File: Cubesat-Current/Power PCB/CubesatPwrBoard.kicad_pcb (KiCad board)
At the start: 2 copper layers, 90 x 96 mm, 92 parts, among them J1 Conn_01x04_Female, J10 S1, J11 S2, J12 S3, J13 S4, J14 S5, J15 S6, J2 Conn_01x04_Female, J3 Conn_01x04_Female, J5 Conn_01x04_Female, J6 Conn_01x03_Female, J7 Conn_01x03_Female, J8 Conn_01x03_Female, Q1 TQM110NB04CR_RLG, Q2 2N7002*, Q3 TQM110NB04CR_RLG, Q4 2N7002*, Q5 TQM110NB04CR_RLG, Q6 2N7002*, U1 LTC4162, U2 LTC4162, U3 LTC4162, U5 MAX710ESE+T, U6 MAX710ESE+T, U7 MAX710ESE+T

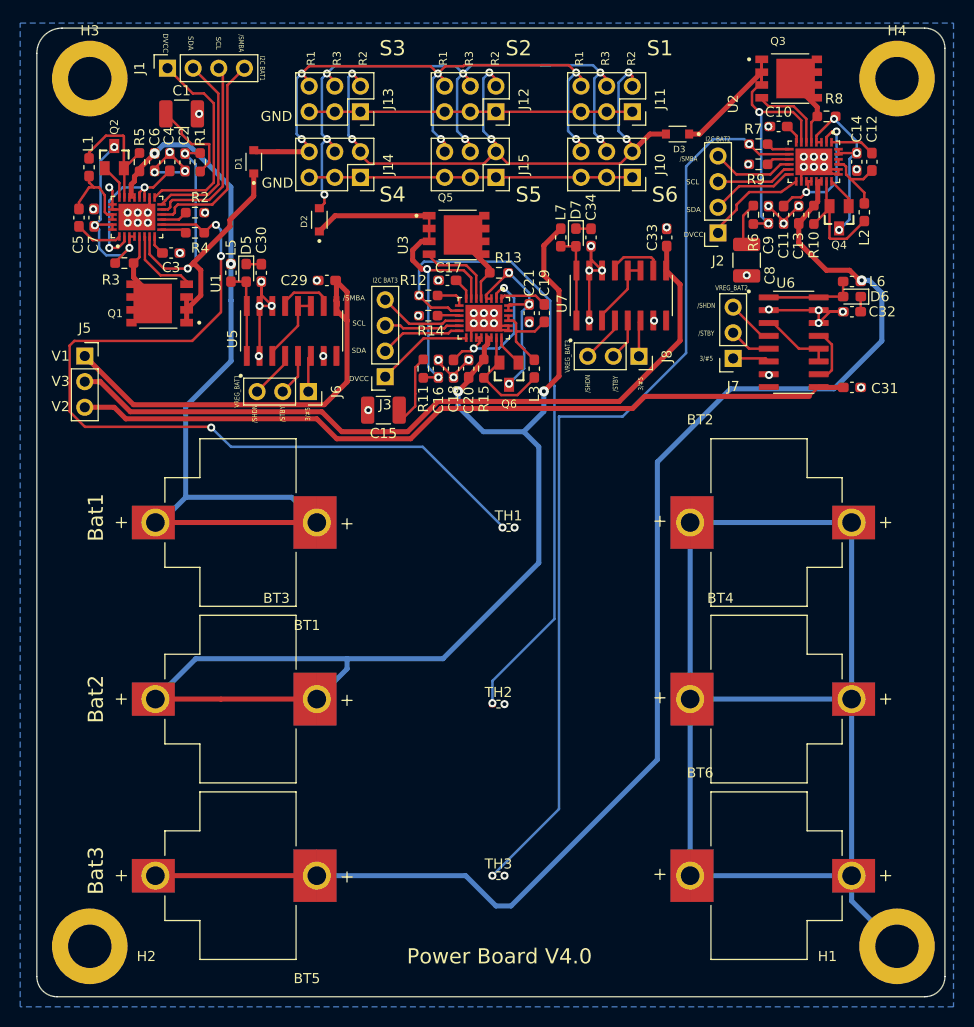
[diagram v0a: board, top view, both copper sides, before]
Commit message: Changed mounting holes to 4.2mm diameter and added silkscreen text
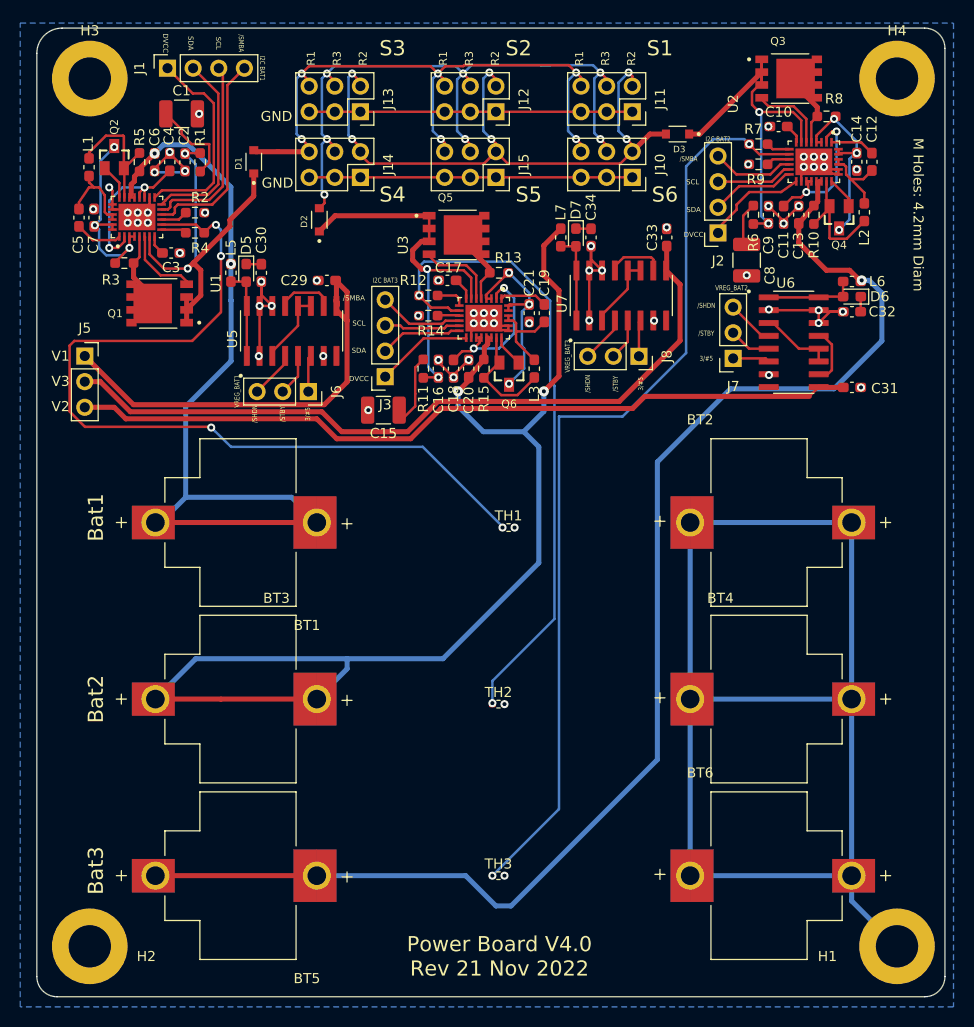
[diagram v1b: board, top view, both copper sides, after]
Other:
- board text added: "M Holes: 4.2mm Diam"
- board text added: "Power Board V4.0 Rev 21 Nov 2022"
- board text removed: "Power Board V4.0"
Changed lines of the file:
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@@
     (fp_circle (center 0 0) (end 3.75 0) (layer "Cmts.User") (width 0.15) (fill none))
     (fp_circle (center 0 0) (end 4 0) (layer "F.CrtYd") (width 0.05) (fill none))
-    (pad "1" thru_hole circle (at 0 0) (size 7.5 7.5) (drill 4.3) (layers *.Cu *.Paste *.Mask)
+    (pad "1" thru_hole circle (at 0 0) (size 7.5 7.5) (drill 4.2) (layers *.Cu *.Paste *.Mask)
       (net 2 "GND") (pinfunction "1") (pintype "input"))
   )
@@
     (fp_circle (center 0 0) (end 3.75 0) (layer "Cmts.User") (width 0.15) (fill none))
     (fp_circle (center 0 0) (end 4 0) (layer "F.CrtYd") (width 0.05) (fill none))
-    (pad "1" thru_hole circle (at 0 0) (size 7.5 7.5) (drill 4.3) (layers *.Cu *.Paste *.Mask)
+    (pad "1" thru_hole circle (at 0 0) (size 7.5 7.5) (drill 4.2) (layers *.Cu *.Paste *.Mask)
       (net 2 "GND") (pinfunction "1") (pintype "input"))
   )
@@
     (fp_circle (center 0 0) (end 3.75 0) (layer "Cmts.User") (width 0.15) (fill none))
     (fp_circle (center 0 0) (end 4 0) (layer "F.CrtYd") (width 0.05) (fill none))
-    (pad "1" thru_hole circle (at 0 0) (size 7.5 7.5) (drill 4.3) (layers *.Cu *.Paste *.Mask)
+    (pad "1" thru_hole circle (at 0 0) (size 7.5 7.5) (drill 4.2) (layers *.Cu *.Paste *.Mask)
       (net 2 "GND") (pinfunction "1") (pintype "input"))
   )
@@
     (fp_circle (center 0 0) (end 3.75 0) (layer "Cmts.User") (width 0.15) (fill none))
     (fp_circle (center 0 0) (end 4 0) (layer "F.CrtYd") (width 0.05) (fill none))
-    (pad "1" thru_hole circle (at 0 0) (size 7.5 7.5) (drill 4.3) (layers *.Cu *.Paste *.Mask)
+    (pad "1" thru_hole circle (at 0 0) (size 7.5 7.5) (drill 4.2) (layers *.Cu *.Paste *.Mask)
       (net 2 "GND") (pinfunction "1") (pintype "input"))
   )
@@
     (effects (font (size 0.5 0.5) (thickness 0.125)))
   )
-  (gr_text "Power Board V4.0" (at 152.5 137.5) (layer "F.SilkS")
+  (gr_text "Power Board V4.0\nRev 21 Nov 2022" (at 152.5 137.5) (layer "F.SilkS")
     (effects (font (size 1.5 1.5) (thickness 0.3)))
   )
@@
     (effects (font (size 0.5 0.4) (thickness 0.1)))
   )
+  (gr_text "M Holes: 4.2mm Diam" (at 194 64 270) (layer "F.SilkS")
+    (effects (font (size 1 1) (thickness 0.15)))
+  )
   (gr_text "3/#5" (at 166.5 80.75 90) (layer "F.SilkS")

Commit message: Updating to revision 5.0
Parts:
- removed BT1, BT2, BT3, BT4: 254TR, 254TR:BAT_254TR
- removed C19: C, Capacitor_SMD:C_0603_1608Metric_Pad1.08x0.95mm_HandSolder
- removed C20, C21: 10u, Capacitor_SMD:C_0603_1608Metric_Pad1.08x0.95mm_HandSolder
- removed C29, C30: C_Polarized_US, Capacitor_SMD:C_0603_1608Metric_Pad1.08x0.95mm_HandSolder
- removed C31, C33: 4.7u, Capacitor_SMD:C_0603_1608Metric_Pad1.08x0.95mm_HandSolder
- removed C32, C34: 100u, Capacitor_SMD:C_0603_1608Metric_Pad1.08x0.95mm_HandSolder
- removed the D2 at (134.7, 64.5)
- removed D5, D6, D7: D_Schottky, Diode_SMD:D_0603_1608Metric_Pad1.05x0.95mm_HandSolder
- removed the J5 at (111.4, 78.0)
- removed the J6 at (133.6, 81.5)
- removed L5: L, Inductor_SMD:L_0603_1608Metric_Pad1.05x0.95mm_HandSolder
- removed L6, L7: 22u, Inductor_SMD:L_0603_1608Metric_Pad1.05x0.95mm_HandSolder
- removed Q5: TQM110NB04CR_RLG, TQM110N:TRANS_TQM110NB04CR_RLG
- removed Q6: 2N7002*, 2N7002:SOT23
- removed R11: 2.5, Resistor_SMD:R_0603_1608Metric_Pad0.98x0.95mm_HandSolder
- removed R12, R13: 16m, Resistor_SMD:R_0603_1608Metric_Pad0.98x0.95mm_HandSolder
- removed R14: 63.4k, Resistor_SMD:R_0603_1608Metric_Pad0.98x0.95mm_HandSolder
- removed R15: 10m, Resistor_SMD:R_0603_1608Metric_Pad0.98x0.95mm_HandSolder
- removed the TH2 at (152.4, 112.5)
- removed U5, U6, U7: MAX710ESE+T, MAX710ESE:SOIC127P600X175-16N
- added D3: D_Schottky, Connectors_Cubesat_Custom:CubeSat_Diode_SOT_882, F.Cu at (139.4, 71.2)
- added D4: D_Schottky, Connectors_Cubesat_Custom:CubeSat_Diode_SOT_882, F.Cu at (183.1, 69.8)
- added J4: 254TR, 254TR:BAT_254TR, F.Cu at (178.5, 105.0)
- added J9: Conn_01x02_Female, Connectors_Cubesat_Custom:CubeSat_Conn_2x01_P2.54mm, F.Cu at (180.0, 53.0)
- added L4: 22u, Inductor_SMD:L_0603_1608Metric_Pad1.05x0.95mm_HandSolder, F.Cu at (180.6, 69.8)
- added U4: MAX710ESE+T, MAX710ESE:SOIC127P600X175-16N, F.Cu at (187.3, 79.6)
- C1: value C_Polarized_US -> 150u
- C12, C5: value C -> 22n
- C15: value 150u -> 4.7u; footprint Capacitor_SMD:C_1210_3225Metric_Pad1.33x2.70mm_HandSolder -> Capacitor_SMD:C_0603_1608Metric_Pad1.08x0.95mm_HandSolder
- C16: value C_Polarized_US -> 100u; footprint Capacitor_SMD:C_0603_1608Metric_Pad1.08x0.95mm_HandSolder -> Capacitor_SMD:C_0805_2012Metric_Pad1.18x1.45mm_HandSolder
- C17: value 1u -> 4.7u
- C18: value 4.7u -> 100u; footprint Capacitor_SMD:C_0603_1608Metric_Pad1.08x0.95mm_HandSolder -> Capacitor_SMD:C_0805_2012Metric_Pad1.18x1.45mm_HandSolder
- C2, C9: value C_Polarized_US -> 0.1u
- C3: value C -> 1u
- C4: value C -> 4.7u
- C6, C7: value C -> 10u
- D1: footprint CUS520,H3F:DIO_CUS520,H3F -> Connectors_Cubesat_Custom:CubeSat_DIO_CUS520,H3f
- D2: renamed from D3; footprint CUS520,H3F:DIO_CUS520,H3F -> Connectors_Cubesat_Custom:CubeSat_DIO_CUS520,H3f
- H1: renamed from H2; footprint MountingHole:MountingHole_4.3mm_M4_DIN965_Pad -> Connectors_Cubesat_Custom:CubeSat_MountingHole_M4
- H2: renamed from H4; footprint MountingHole:MountingHole_4.3mm_M4_DIN965_Pad -> Connectors_Cubesat_Custom:CubeSat_MountingHole_M4
- H3: renamed from H1; footprint MountingHole:MountingHole_4.3mm_M4_DIN965_Pad -> Connectors_Cubesat_Custom:CubeSat_MountingHole_M4
- H4: renamed from H3; footprint MountingHole:MountingHole_4.3mm_M4_DIN965_Pad -> Connectors_Cubesat_Custom:CubeSat_MountingHole_M4
- J1, J2: footprint Connector_PinSocket_2.54mm:PinSocket_1x04_P2.54mm_Vertical -> Connectors_Cubesat_Custom:CubeSat_Conn_4x01_P2.54mm
- J10, J11, J12, J13, J14, J15: footprint Connector_PinSocket_2.54mm:PinSocket_2x03_P2.54mm_Vertical -> Connectors_Cubesat_Custom:CubeSat_Conn_2x02_P2.54mm
- J3: value Conn_01x04_Female -> 254TR; footprint Connector_PinSocket_2.54mm:PinSocket_1x04_P2.54mm_Vertical -> 254TR:BAT_254TR
- J7, J8: footprint Connector_PinSocket_2.54mm:PinSocket_1x03_P2.54mm_Vertical -> Connectors_Cubesat_Custom:CubeSat_Conn_3x01_P2.54mm
- L1: value L -> 4.7u
- L3: value 4.7u -> 22u
- Q2, Q4: footprint 2N7002:SOT23 -> Connectors_Cubesat_Custom:CubeSat_2n7002
- R1: value R -> 2.5
- R2: value R -> 10k
- R3: value R -> 16m
- R4: value R -> 63.4k
- R5: value R -> 10m
- R7: value 16m -> 10k
- U3: value LTC4162 -> MAX710ESE+T; footprint LTC4162:QFN50P500X400X80-29N -> MAX710ESE:SOIC127P600X175-16N
- moved C17 44.3 mm to (191.6, 69.8), turned to 90 degrees
- moved R8 39.1 mm to (168.3, 89.6), turned to -90 degrees
- moved C12 38.9 mm to (165.8, 89.6)
- moved C18 38.6 mm to (185.4, 69.8)
- moved C14 37.5 mm to (171.8, 92.6), turned to 0 degrees
- moved L2 36.4 mm to (163.0, 89.6)
- moved Q3 35.7 mm to (172.7, 85.2), turned to -90 degrees
- moved Q4 35.6 mm to (159.5, 87.9)
- moved C13 35.3 mm to (153.5, 84.7), turned to -90 degrees
- moved J7 34.7 mm to (143.0, 90.0), turned to -90 degrees
- moved R10 34.3 mm to (156.3, 84.7)
- moved J3 29.5 mm to (125.5, 105.0)
- moved U2 29.2 mm to (163.8, 80.1), turned to 180 degrees
- moved C11 28.9 mm to (156.3, 79.6), turned to 90 degrees
- moved C7 28.2 mm to (128.9, 87.0), turned to 0 degrees
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- renumbered BT5 to J5, BT6 to J6, TH3 to TH2
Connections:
- net /Bat_Reg_1/DVCC renamed /Bat_Reg_4/DVCC
- net /Bat_Reg_1/SCL renamed /Bat_Reg_4/SCL
- net /Bat_Reg_1/SDA renamed /Bat_Reg_4/SDA
- net /Bat_Reg_1/TH renamed /Bat_Reg_4/TH
- net /Bat_Reg_1/VIN renamed /Bat_Reg_4/VIN
- net /Bat_Reg_1//SMBALERT renamed /Bat_Reg_4//SMBALERT
- net Net-(C14-Pad1) renamed /Bat_Reg_3/V_Out
- C15 pad 1: Net-(C15-Pad1) -> /V_Reg_3.3_5V4/Vout
- C16 pad 1: /Bat_Reg_2/VIN -> Net-(C16-Pad1)
- C17 pad 1: GND -> /V_Reg_3.3_5V3/Vout
- C17 pad 2: Net-(C17-Pad2) -> GND
- C6 pad 1: /Bat_Reg_1/V_Bat -> /Bat_Reg_4/V_Bat
- C7 pad 1: Net-(C7-Pad1) -> /Bat_Reg_4/V_Out
- D2 pad 2: Net-(D3-Pad2) -> Net-(D2-Pad2)
- J10 pad 1: GND -> Net-(D2-Pad2)
- J10 pad 2: Net-(D3-Pad2) -> GND
- J10 pad 3: GND -> Net-(D1-Pad2)
- J10 pad 4: Net-(D2-Pad2) -> GND
- J11 pad 1: GND -> Net-(D2-Pad2)
- J11 pad 2: Net-(D3-Pad2) -> GND
- J11 pad 3: GND -> Net-(D1-Pad2)
- J11 pad 4: Net-(D2-Pad2) -> GND
- J12 pad 1: GND -> Net-(D2-Pad2)
- J12 pad 2: Net-(D3-Pad2) -> GND
- J12 pad 3: GND -> Net-(D1-Pad2)
- J12 pad 4: Net-(D2-Pad2) -> GND
- J13 pad 1: GND -> Net-(D2-Pad2)
- J13 pad 2: Net-(D3-Pad2) -> GND
- J13 pad 3: GND -> Net-(D1-Pad2)
- J13 pad 4: Net-(D2-Pad2) -> GND
- J14 pad 1: GND -> Net-(D2-Pad2)
- J14 pad 2: Net-(D3-Pad2) -> GND
- J14 pad 3: GND -> Net-(D1-Pad2)
- J14 pad 4: Net-(D2-Pad2) -> GND
- J15 pad 1: GND -> Net-(D2-Pad2)
- J15 pad 2: Net-(D3-Pad2) -> GND
- J15 pad 3: GND -> Net-(D1-Pad2)
- J15 pad 4: Net-(D2-Pad2) -> GND
- J7 pad 1: /V_Reg_3.3_5V3/3/#5 -> /V_Reg_3.3_5V4/3/#5
- J7 pad 2: /V_Reg_3.3_5V3/#STBY -> /V_Reg_3.3_5V4/#STBY
- J7 pad 3: /V_Reg_3.3_5V3/#SHDN -> /V_Reg_3.3_5V4/#SHDN
- J8 pad 1: /V_Reg_3.3_5V2/3/#5 -> /V_Reg_3.3_5V3/3/#5
- J8 pad 2: /V_Reg_3.3_5V2/#STBY -> /V_Reg_3.3_5V3/#STBY
- J8 pad 3: /V_Reg_3.3_5V2/#SHDN -> /V_Reg_3.3_5V3/#SHDN
- L3 pad 1: Net-(C19-Pad2) -> /Bat_Reg_4/V_Out
- L3 pad 2: Net-(L3-Pad2) -> Net-(D3-Pad2)
- Q2 pad 3: Net-(C7-Pad1) -> /Bat_Reg_4/V_Out
- R3 pad 1: Net-(C7-Pad1) -> /Bat_Reg_4/V_Out
- R5 pad 1: /Bat_Reg_1/V_Bat -> /Bat_Reg_4/V_Bat
- U1 pad 19: /Bat_Reg_1/V_Bat -> /Bat_Reg_4/V_Bat
- U1 pad 20: /Bat_Reg_1/V_Bat -> /Bat_Reg_4/V_Bat
- U1 pad 27: Net-(C7-Pad1) -> /Bat_Reg_4/V_Out
- U1 pad 28: Net-(C7-Pad1) -> /Bat_Reg_4/V_Out
- U1 pad 3: Net-(C7-Pad1) -> /Bat_Reg_4/V_Out
- U1 pad 4: Net-(C7-Pad1) -> /Bat_Reg_4/V_Out
- U3 pad 1: Net-(C19-Pad1) -> Net-(D3-Pad2)
- U3 pad 10: /Bat_Reg_2/TH -> Net-(U3-Pad10)
- U3 pad 11: Net-(R14-Pad2) -> Net-(U3-Pad11)
- U3 pad 12: /Bat_Reg_2//SMBALERT -> Net-(U3-Pad11)
- U3 pad 13: /Bat_Reg_2/SCL -> Net-(U3-Pad10)
- U3 pad 14: /Bat_Reg_2/SDA -> GND
- U3 pad 15: /Bat_Reg_2/DVCC -> GND
- U3 pad 16: GND -> Net-(D3-Pad2)
- U3 pad 2: Net-(C18-Pad1) -> GND
- U3 pad 3: Net-(C21-Pad1) -> Net-(U3-Pad11)
- U3 pad 4: Net-(C21-Pad1) -> /V_Reg_3.3_5V4/#SHDN
- U3 pad 5: Net-(Q5-Pad5_8) -> /V_Reg_3.3_5V4/#STBY
- U3 pad 6: Net-(Q5-Pad4) -> /V_Reg_3.3_5V4/3/#5
- U3 pad 7: /Bat_Reg_2/VIN -> GND
- U3 pad 8: Net-(C17-Pad2) -> unconnected-(U3-Pad8)
- U3 pad 9: Net-(R12-Pad1) -> /V_Reg_3.3_5V4/Vout
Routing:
- net /Bat_Reg_2/V_Bat: track 117.6 -> 0.00 mm, vias 2 -> 0
- net /Bat_Reg_1/V_Bat: track 81.9 -> 0.00 mm, vias 2 -> 0
- net /V_Reg_3.3_5V2/Vout: track 74.8 -> 0.00 mm
- net /Bat_Reg_2/TH: track 64.9 -> 0.00 mm, vias 2 -> 0
- net /Bat_Reg_3/V_Bat: track 136.4 -> 77.4 mm, vias 1 -> 0
- net /Bat_Reg_4/V_Bat: track 0.00 -> 56.2 mm
- net /V_Reg_3.3_5V3/Vout: track 78.6 -> 27.3 mm
- net /Bat_Reg_4/V_Out: track 0.00 -> 48.9 mm, vias 0 -> 4
- net Net-(D3-Pad2): track 63.7 -> 15.0 mm, vias 6 -> 0
- net /V_Reg_3.3_5V4/Vout: track 0.00 -> 45.2 mm, vias 0 -> 2
- net /V_Reg_3.3_5V1/Vout: track 44.9 -> 0.00 mm
- net /Bat_Reg_2/VIN: track 38.6 -> 0.00 mm, vias 2 -> 0
- net /Bat_Reg_3/V_Out: track 18.7 -> 52.5 mm, vias 3 -> 4
- net /Bat_Reg_4/TH: track 85.6 -> 57.0 mm, vias 4 -> 2
- net GND: track 263.0 -> 235.2 mm, vias 61 -> 30
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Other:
- board text added: "B1 B2"
- board text added: "OUT"
- board text added: "Power Board V5.0 Rev 3 April 2023"
- board text removed: "/SHDN"
- board text removed: "/SMBA"
- board text removed: "/STBY"
- board text removed: "3/#5"
- board text removed: "Bat3"
- board text removed: "DVCC"
- board text removed: "GND"
- board text removed: "I2C BAT1"
- board text removed: "I2C BAT2"
- board text removed: "I2C BAT3"
- board text removed: "Power Board V4.0 Rev 21 Nov 2022"
- board text removed: "R1 R3 R2"
- board text removed: "SCL"
- board text removed: "SDA"
- board text removed: "V1"
- board text removed: "V2"
- board text removed: "V3"
- board text removed: "VREG_BAT1"
- board text removed: "VREG_BAT2"
- board text removed: "VREG_BAT3"

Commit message: Final update for version 5, should be ready for shipping out
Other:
- board text added: "/SMBALRT"
- board text added: "B1"
- board text added: "B2"
- board text added: "DVCC"
- board text added: "SCL"
- board text added: "SDA"
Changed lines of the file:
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@@
   (gr_circle (center 111.9 50.5) (end 113.928486 50.5) (layer "F.Paste") (width 0.12) (fill solid))
   (gr_line (start 111 125.5) (end 111 129.5) (layer "F.SilkS") (width 0.5))
-  (gr_line (start 109 93) (end 109 58) (layer "F.SilkS") (width 0.12))
+  (gr_line (start 109 94.6) (end 109 58) (layer "F.SilkS") (width 0.12))
   (gr_line (start 174 60) (end 174 64) (layer "F.SilkS") (width 0.12))
-  (gr_line (start 152 64) (end 152 95) (layer "F.SilkS") (width 0.12))
-  (gr_line (start 150 65) (end 150 93) (layer "F.SilkS") (width 0.12))
+  (gr_line (start 152 64) (end 152 96) (layer "F.SilkS") (width 0.12))
+  (gr_line (start 150 65) (end 150 94.6) (layer "F.SilkS") (width 0.12))
   (gr_line (start 191 105) (end 194.5 105) (layer "F.SilkS") (width 0.5))
   (gr_line (start 109 58) (end 136 58) (layer "F.SilkS") (width 0.12))
   (gr_line (start 109.5 105) (end 113 105) (layer "F.SilkS") (width 0.5))
-  (gr_line (start 152 95) (end 195 95) (layer "F.SilkS") (width 0.12))
+  (gr_line (start 152 96) (end 195 96) (layer "F.SilkS") (width 0.12))
   (gr_line (start 136 65) (end 150 65) (layer "F.SilkS") (width 0.12))
   (gr_line (start 195 60) (end 174 60) (layer "F.SilkS") (width 0.12))
   (gr_line (start 174 64) (end 152 64) (layer "F.SilkS") (width 0.12))
-  (gr_line (start 195 95) (end 195 60) (layer "F.SilkS") (width 0.12))
+  (gr_line (start 195 96) (end 195 60) (layer "F.SilkS") (width 0.12))
   (gr_line (start 111.25 103) (end 111.25 107) (layer "F.SilkS") (width 0.5))
   (gr_line (start 109.25 127.5) (end 112.75 127.5) (layer "F.SilkS") (width 0.5))
   (gr_line (start 136 58) (end 136 65) (layer "F.SilkS") (width 0.12))
-  (gr_line (start 150 93) (end 109 93) (layer "F.SilkS") (width 0.12))
+  (gr_line (start 150 94.6) (end 109 94.6) (layer "F.SilkS") (width 0.12))
   (gr_line (start 190.75 127.5) (end 194.25 127.5) (layer "F.SilkS") (width 0.5))
   (gr_line (start 106.65 139.5) (end 106.65 48) (layer "Edge.Cuts") (width 0.05))
@@
     (effects (font (size 1 1) (thickness 0.15)))
   )
+  (gr_text "DVCC" (at 186.9 94 315) (layer "F.SilkS")
+    (effects (font (size 0.75 0.75) (thickness 0.15)))
+  )
+  (gr_text "SDA" (at 144 92.8 315) (layer "F.SilkS")
+    (effects (font (size 0.75 0.75) (thickness 0.15)))
+  )
+  (gr_text "B2" (at 146.25 52.75) (layer "F.SilkS")
+    (effects (font (size 1 1) (thickness 0.15)))
+  )
+  (gr_text "DVCC" (at 155.6 68.3 45) (layer "F.SilkS")
+    (effects (font (size 0.75 0.75) (thickness 0.15)))
+  )
+  (gr_text "SDA" (at 116 63.7 45) (layer "F.SilkS")
+    (effects (font (size 0.75 0.75) (thickness 0.15)))
+  )
+  (gr_text "/SMBALRT" (at 122.2 62.3 45) (layer "F.SilkS")
+    (effects (font (size 0.75 0.75) (thickness 0.15)))
+  )
   (gr_text "B1 B2" (at 180 50.5) (layer "F.SilkS")
     (effects (font (size 1 1) (thickness 0.15)))
@@
     (effects (font (size 1.5 1.5) (thickness 0.3)))
   )
+  (gr_text "SCL" (at 146.5 92.8 315) (layer "F.SilkS")
+    (effects (font (size 0.75 0.75) (thickness 0.15)))
+  )
+  (gr_text "SCL" (at 160.6 68.5 45) (layer "F.SilkS")
+    (effects (font (size 0.75 0.75) (thickness 0.15)))
+  )
   (gr_text "S3" (at 141.825 47.22) (layer "F.SilkS")
     (effects (font (size 1.5 1.5) (thickness 0.3)))
   )
-  (gr_text "Bat1" (at 113 61) (layer "F.SilkS")
+  (gr_text "Bat1" (at 112.5 60) (layer "F.SilkS")
     (effects (font (size 1.5 1.5) (thickness 0.3)))
+  )
+  (gr_text "DVCC" (at 113.5 63.4 45) (layer "F.SilkS")
+    (effects (font (size 0.75 0.75) (thickness 0.15)))
+  )
+  (gr_text "SCL" (at 118.5 63.7 45) (layer "F.SilkS")
+    (effects (font (size 0.75 0.75) (thickness 0.15)))
   )
   (gr_text "S4" (at 142.325 62.22) (layer "F.SilkS")
@@
     (effects (font (size 1.5 1.5) (thickness 0.3)))
   )
+  (gr_text "DVCC" (at 141.5 93.1 315) (layer "F.SilkS")
+    (effects (font (size 0.75 0.75) (thickness 0.15)))
+  )
+  (gr_text "SDA" (at 189.4 93.7 315) (layer "F.SilkS")
+    (effects (font (size 0.75 0.75) (thickness 0.15)))
+  )
   (gr_text "Bat2\n" (at 191 63) (layer "F.SilkS")
     (effects (font (size 1.5 1.5) (thickness 0.3)))
+  )
+  (gr_text "SDA" (at 158.1 68.5 45) (layer "F.SilkS")
+    (effects (font (size 0.75 0.75) (thickness 0.15)))
   )
   (gr_text "S5" (at 155.825 62.22) (layer "F.SilkS")
@@
     (effects (font (size 1.5 1.5) (thickness 0.3)))
   )
+  (gr_text "/SMBALRT" (at 164.4 67.1 45) (layer "F.SilkS")
+    (effects (font (size 0.75 0.75) (thickness 0.15)))
+  )
   (gr_text "Bat1" (at 111.5 109) (layer "F.SilkS")
     (effects (font (size 1.5 1.5) (thickness 0.3)))
@@
     (effects (font (size 1.5 1.5) (thickness 0.3)))
   )
+  (gr_text "B1" (at 138 52.75) (layer "F.SilkS")
+    (effects (font (size 1 1) (thickness 0.15)))
+  )
+  (gr_text "SCL" (at 191.9 93.7 315) (layer "F.SilkS")
+    (effects (font (size 0.75 0.75) (thickness 0.15)))
+  )
   (gr_text "M Holes: 4.2mm Diam" (at 126.25 52) (layer "F.SilkS")

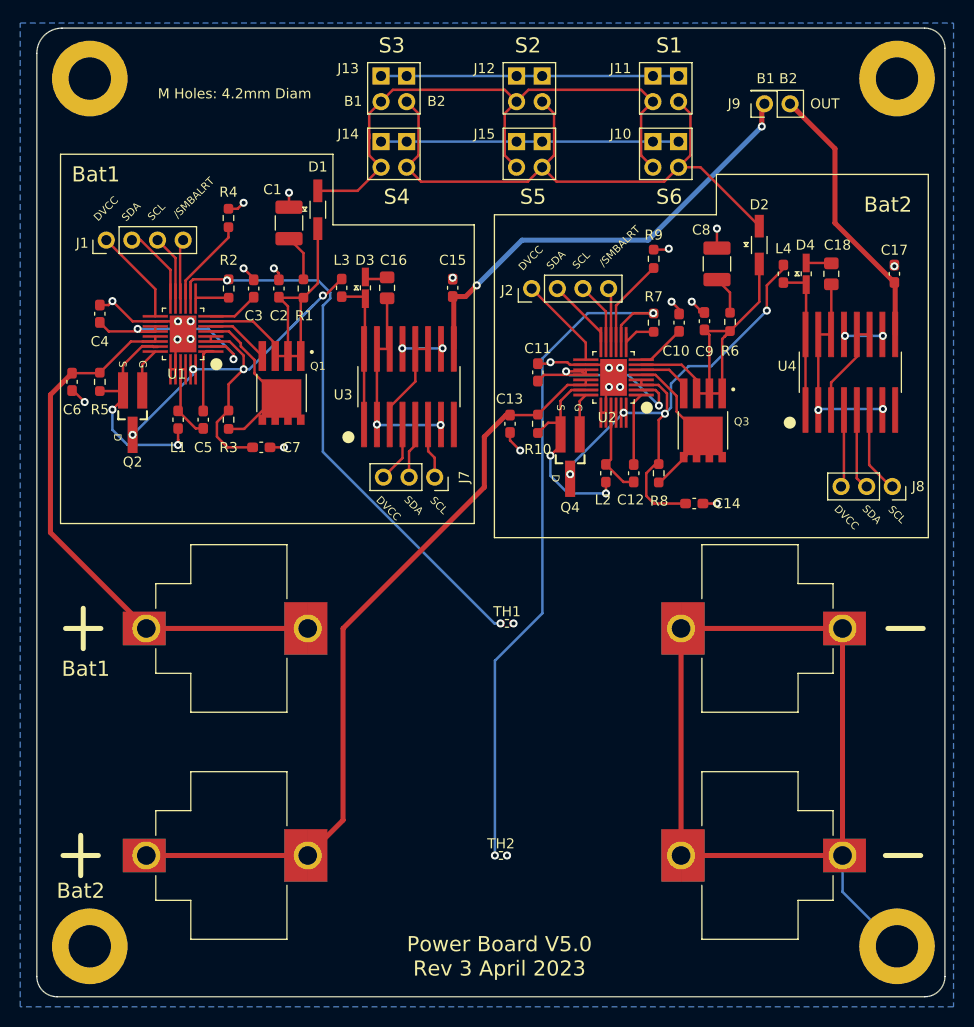
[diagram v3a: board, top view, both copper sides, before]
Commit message: rotated one text and realigned mounting holes
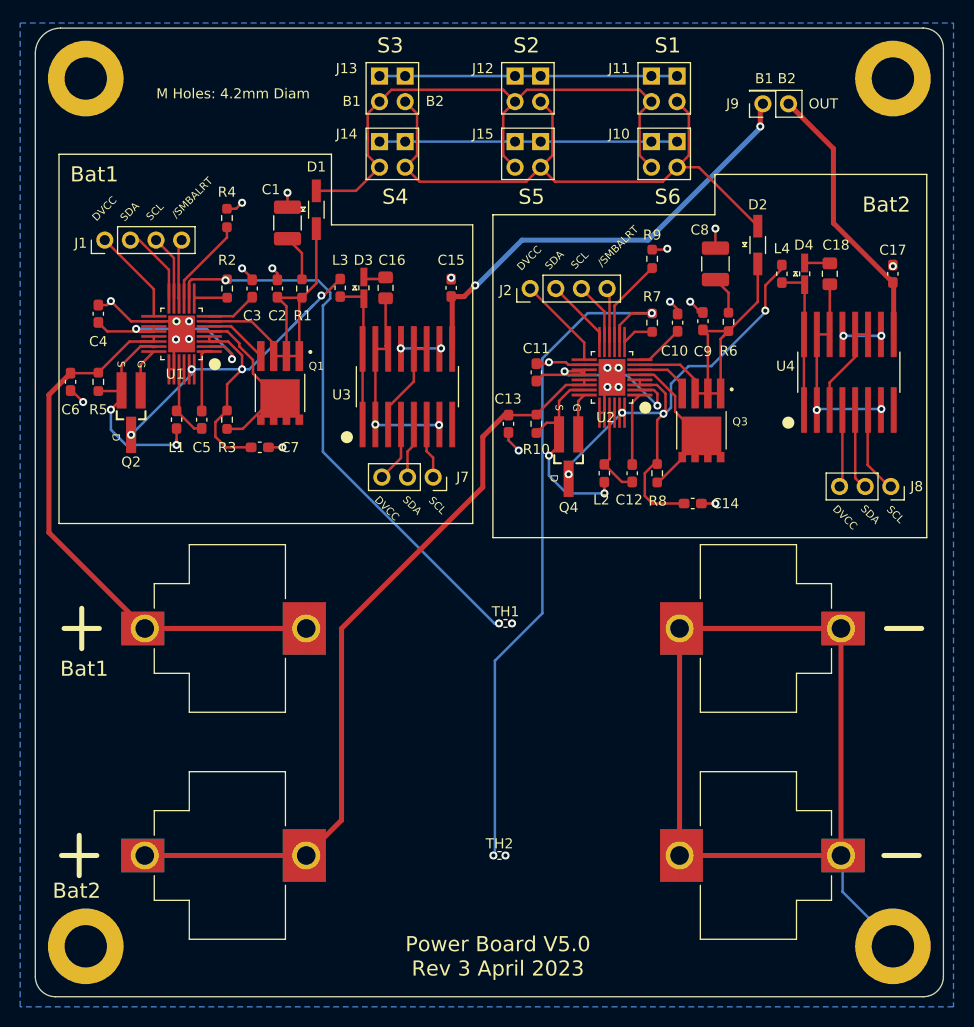
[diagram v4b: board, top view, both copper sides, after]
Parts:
- moved H1 0.40 mm to (111.5, 136.5)
- moved H2 0.40 mm to (191.5, 50.5)
- moved H3 0.40 mm to (191.5, 136.5)
- moved H4 0.40 mm to (111.5, 50.5)
- moved C1 0.15 mm to (131.5, 64.8)
- moved C10 0.15 mm to (170.2, 74.7)
- moved C11 0.15 mm to (156.2, 79.6)
- moved C12 0.15 mm to (165.7, 89.6)
- moved C14 0.15 mm to (171.7, 92.6)
- moved C15 0.15 mm to (147.7, 71.2)
- moved C16 0.15 mm to (141.2, 71.2)
- moved C2 0.15 mm to (130.5, 71.3)
- moved C3 0.15 mm to (128.0, 71.3)
- moved C7 0.15 mm to (128.7, 87.0)
- moved C8 0.15 mm to (173.9, 68.9)
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
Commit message: Added gerbers
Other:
- board text added: "0.1u"
- board text added: "100u"
- board text added: "10k"
- board text added: "10m"
- board text added: "10u"
- board text added: "150u"
- board text added: "16m"
- board text added: "1u"
- board text added: "2.5"
- board text added: "22n"
- board text added: "22u"
- board text added: "2N7"
- board text added: "4.7u"
- board text added: "63.4k"
- board text added: "BAS"
- board text added: "CUS"
- board text added: "TQM"
